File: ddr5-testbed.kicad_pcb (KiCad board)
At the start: 6 copper layers, 69.6 x 30 mm, 64 parts, among them IC1 PCA6408APW, IC2 AT24CS01, J1 ddr4-sodimm-edge-connector, U1 MT60B2G8HB-48B_A, U2 TPS613221ADBVT

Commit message: Added on bottom silkscreen field for serial number
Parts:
- added kibuzzard-623AE55E: G***, label, B.Cu at (112.6, 78.8)

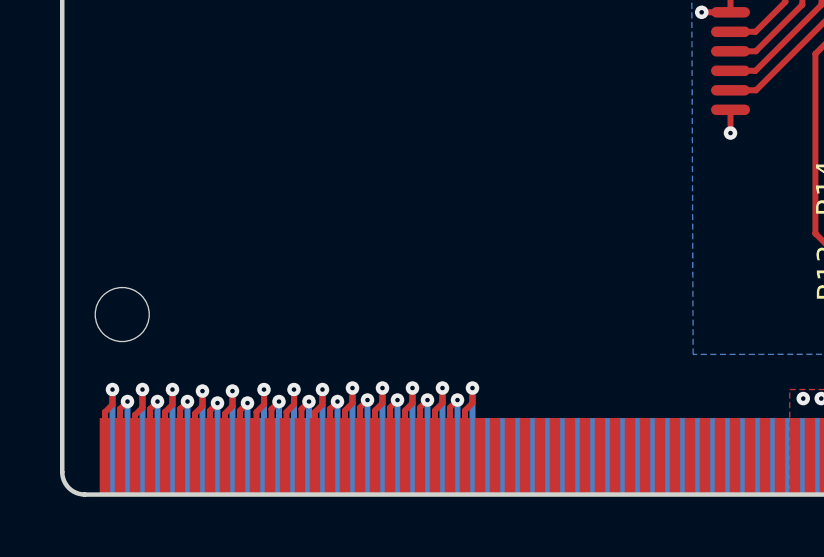
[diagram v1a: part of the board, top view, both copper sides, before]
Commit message: Added PCB SHA string
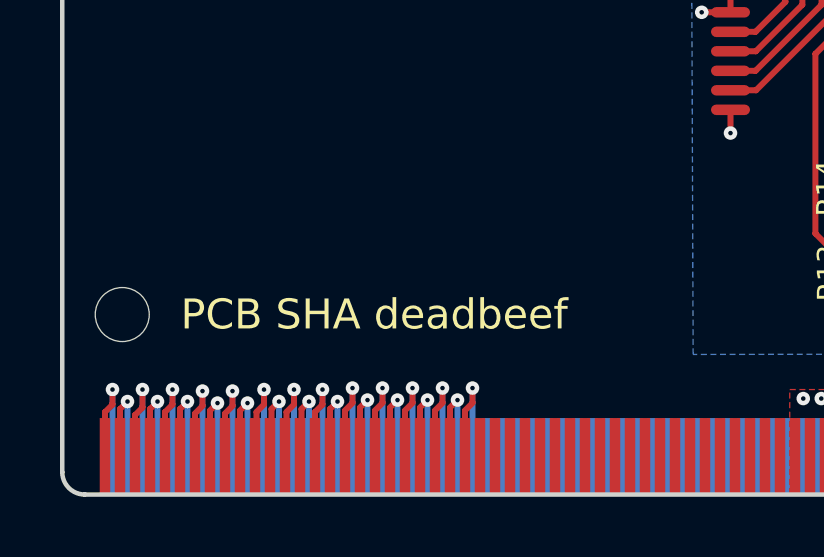
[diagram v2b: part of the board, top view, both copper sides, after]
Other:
- board text added: "PCB SHA deadbeef"
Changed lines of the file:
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@@
     (effects (font (size 0.85 0.85) (thickness 0.18)) (justify left))
+  )
+  (gr_text "PCB SHA deadbeef" (at 110.4 94) (layer "F.SilkS")
+    (effects (font (size 1 1) (thickness 0.15)))
   )
   (gr_text "DDR5 Testbed\nRev. 1.0.2  12/2022" (at 108.525 78.2) (layer "F.Mask")

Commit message: Bump revision to 1.1.0
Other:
- board text added: "DDR5 Testbed Rev. 1.1.0 01/2023"
- board text removed: "DDR5 Testbed Rev. 1.0.2 12/2022"
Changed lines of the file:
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@@
   (gr_arc (start 101.1 78) (mid 101.559619 78.190381) (end 101.75 78.65) (layer "Edge.Cuts") (width 0.15))
   (gr_arc (start 167.85 78.65) (mid 168.040381 78.190381) (end 168.5 78) (layer "Edge.Cuts") (width 0.15))
-  (gr_text "DDR5 Testbed\nRev. 1.0.2  12/2022" (at 108.525 78.2) (layer "F.Cu")
+  (gr_text "DDR5 Testbed\nRev. 1.1.0  01/2023" (at 108.525 78.2) (layer "F.Cu")
     (effects (font (size 0.85 0.85) (thickness 0.18)) (justify left))
   )
-  (gr_text "PCB SHA deadbeef" (at 110.4 94) (layer "F.SilkS")
-    (effects (font (size 1 1) (thickness 0.15)))
+  (gr_text "PCB SHA deadbeef" (at 109 94.02) (layer "F.SilkS")
+    (effects (font (size 0.7 0.7) (thickness 0.15)))
   )
-  (gr_text "DDR5 Testbed\nRev. 1.0.2  12/2022" (at 108.525 78.2) (layer "F.Mask")
+  (gr_text "DDR5 Testbed\nRev. 1.1.0  01/2023" (at 108.525 78.2) (layer "F.Mask")
     (effects (font (size 0.85 0.85) (thickness 0.18)) (justify left))
   )

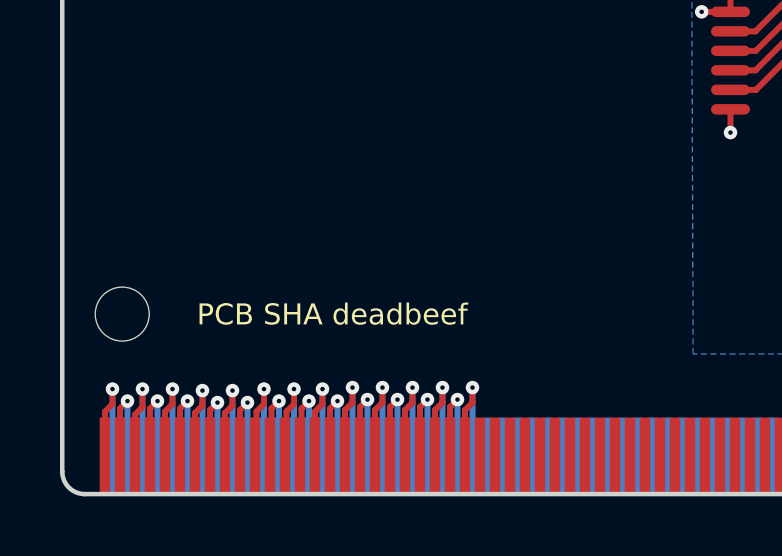
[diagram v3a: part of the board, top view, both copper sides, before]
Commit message: Update PCB marking string
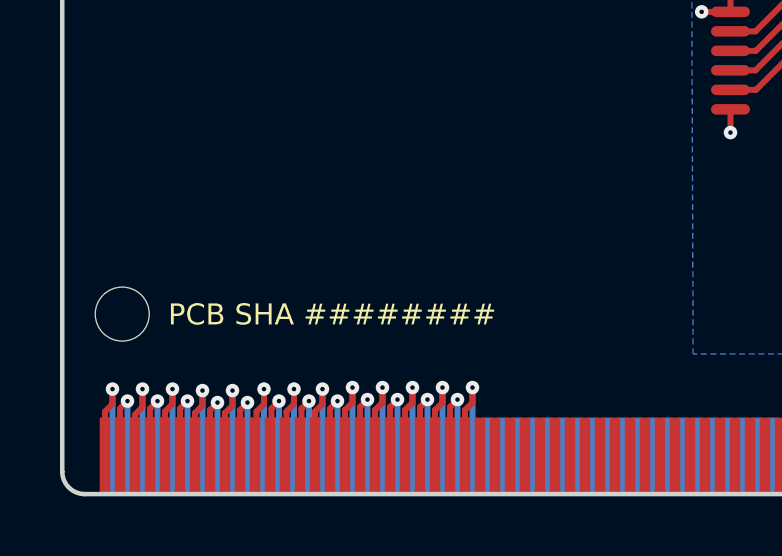
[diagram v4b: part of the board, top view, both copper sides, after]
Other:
- board text added: "PCB SHA ########"
- board text removed: "PCB SHA deadbeef"
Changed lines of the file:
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@@
     (effects (font (size 0.85 0.85) (thickness 0.18)) (justify left))
   )
-  (gr_text "PCB SHA deadbeef" (at 109 94.02) (layer "F.SilkS")
+  (gr_text "PCB SHA ########" (at 109 94.02) (layer "F.SilkS")
     (effects (font (size 0.7 0.7) (thickness 0.15)))
   )

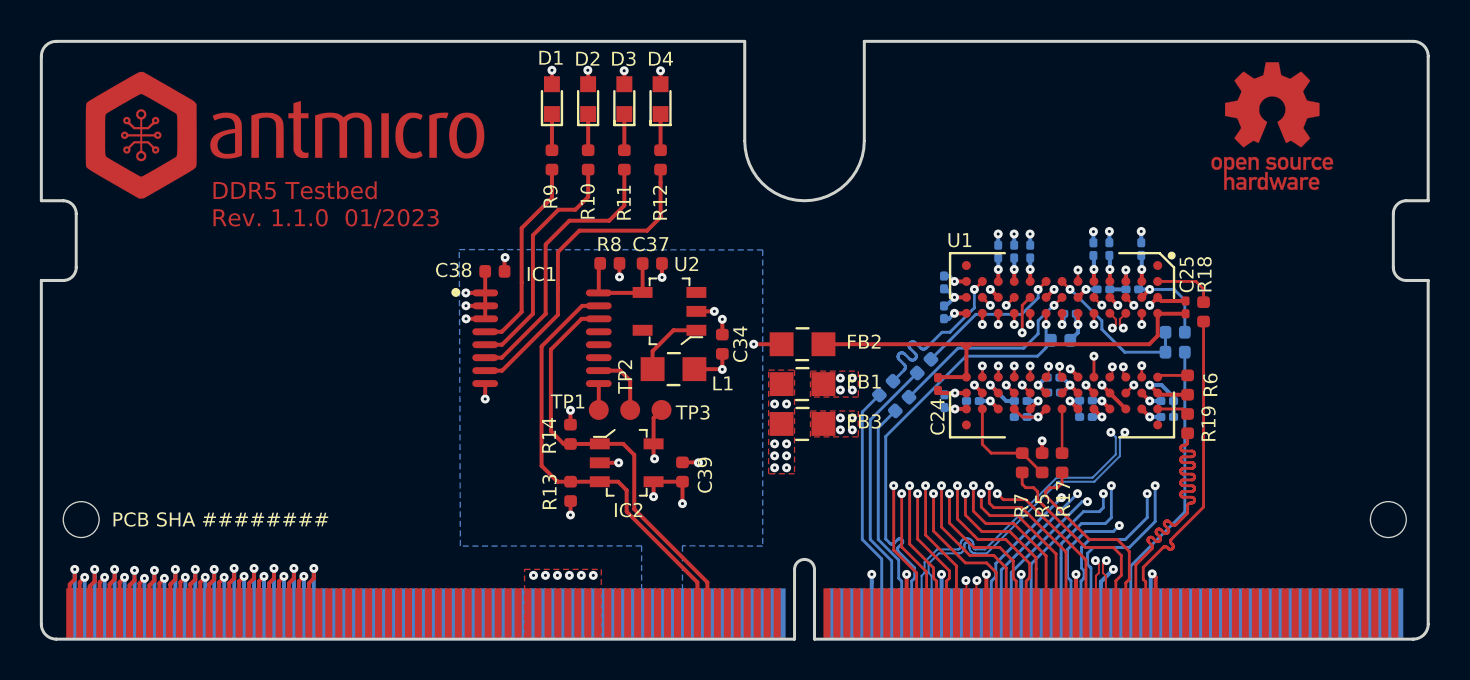
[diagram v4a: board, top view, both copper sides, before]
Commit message: Introduce component standardization
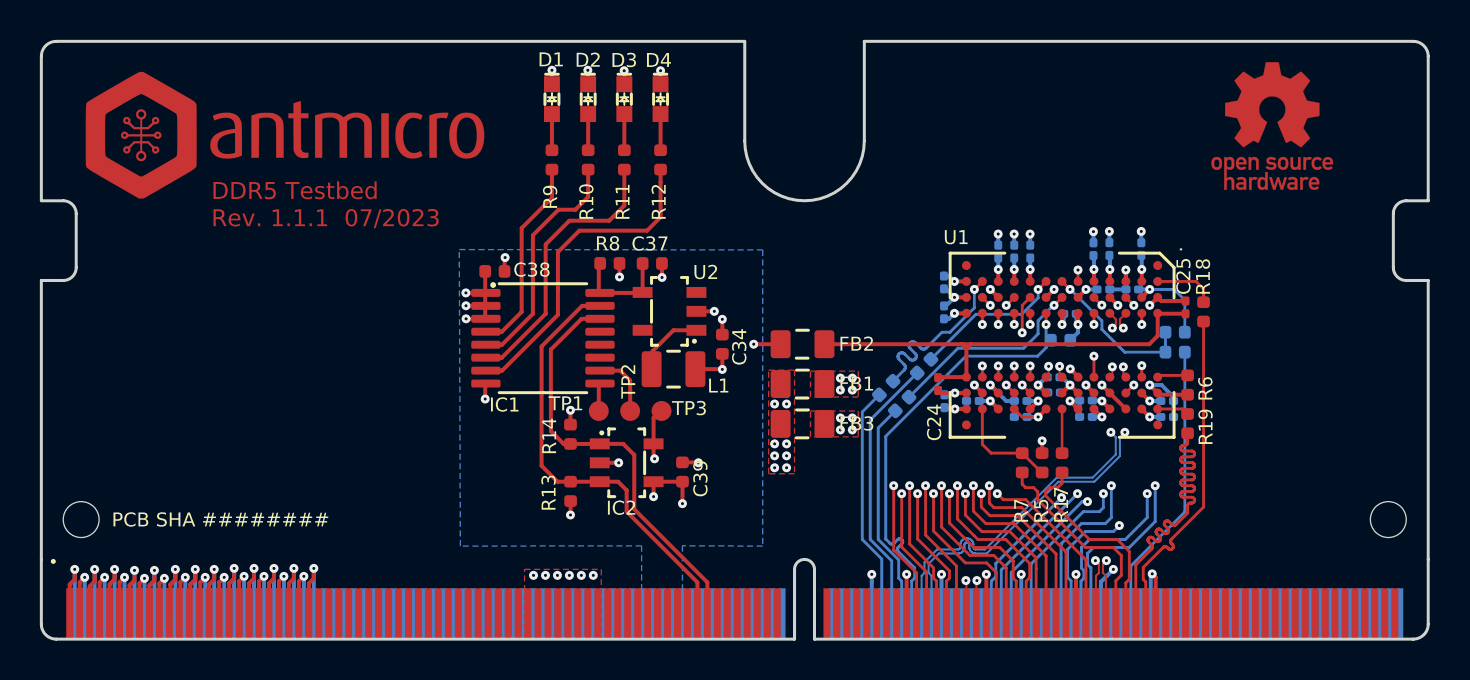
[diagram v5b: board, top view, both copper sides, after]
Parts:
- C1, C10, C11, C12, C13, C14, C15, C18, C2, C23, C24, C25, C26, C28, C3, C30, C32, C4, C5, C6, C7, C8, C9: footprint ddr5-testbed-footprints:0201-res -> ddr5-testbed-footprints:C_0201
- C34, C37, C38, C39: footprint ddr5-testbed-footprints:0402-cap -> ddr5-testbed-footprints:C_0402_1005Metric
- D1, D2, D3, D4: value KP-1608CGCK -> LED_G_0603_KP-1608CGCK; footprint ddr5-testbed-footprints:LED_0603 -> ddr5-testbed-footprints:LED_0603_1608Metric_G
- FB1, FB2, FB3: value 742792022 -> FB_220Z_1.5A_0805; footprint ddr5-testbed-footprints:0805-res -> ddr5-testbed-footprints:FB_0805_2012Metric
- IC1: value PCA6408APW -> PCA6408A_TSSOP; footprint ddr5-testbed-footprints:TSSOP-16 -> ddr5-testbed-footprints:TSSOP-16_4.4x5mm_P0.65mm
- IC2: value AT24CS01 -> AT24CS01_SOT23
- J1: value ddr4-sodimm-edge-connector -> Bus_DDR4_Edge_Conn; footprint ddr5-testbed-footprints:SODIMM_DDR4_EDGE -> ddr5-testbed-footprints:Bus_DDR4_Conn_Edge
- L1: value 1285AS-H-2R2M=P2 -> L_2.2u_1.5A_0806; footprint ddr5-testbed-footprints:0805-res -> ddr5-testbed-footprints:L_0806_2016Metric
- R1, R10, R11, R12, R13, R14, R15, R16, R17, R18, R19, R2, R3, R4, R5, R7, R8, R9: footprint ddr5-testbed-footprints:0402-res -> ddr5-testbed-footprints:R_0402_1005Metric
- R6: value R_240R_1%_0402 -> R_240R_0402; footprint ddr5-testbed-footprints:0402-res -> ddr5-testbed-footprints:R_0402_1005Metric
- TP1, TP2, TP3: value TP_SMD1MM -> TP_1mm_SMD
- U1: footprint ddr5-testbed-footprints:FVBGA-82_11x13_9.0x11.0mm -> ddr5-testbed-footprints:BGA-82_11x9mm_Layout13x11_P0.8mm_DDR5_MO-210-AN
- U2: value TPS613221ADBVT -> TPS613221A_SOT-23-5
- turned IC2 to 0 degrees
- turned U2 to 180 degrees
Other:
- board size 69.6 x 30 mm -> 69.6 x 26 mm
- board text added: "DDR5 Testbed Rev. ${REVISION} 07/2023"
- board text removed: "DDR5 Testbed Rev. 1.1.0 01/2023"
